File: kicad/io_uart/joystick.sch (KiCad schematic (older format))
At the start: 8 parts

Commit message: cleanup
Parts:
- gave numbers to parts that had none: 3
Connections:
- net /JOYPORT_ENABLE: now also U2.5, U2.9; no longer U2.10, U2.12
- net JOYPORT_SELECT: now also U2.1, U2.2, U2.4; no longer U2.4, U2.5, U2.9
- net at U3.19 (OEb), U4.1 (EN): now also U2.6; no longer U2.8
- net at U3.1 (OEa), U4.4 (EN): now also U2.8; no longer U2.11
- new net: U2.10, U2.3
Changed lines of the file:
@@
 	6100 3900 7250 3900
 $Comp
-L 7400 U?
-U 2 1 58E419A1
+L 7400 U2
+U 1 1 58E419A1
 P 3700 3450
-F 0 "U?" H 3700 3500 50  0000 C CNN
+F 0 "U2" H 3700 3500 50  0000 C CNN
 F 1 "7400" H 3700 3350 50  0000 C CNN
 F 2 "" H 3700 3450 50  0000 C CNN
 F 3 "" H 3700 3450 50  0000 C CNN
-	2    3700 3450
-	1    0    0    -1
-$EndComp
-$Comp
-L 7400 U?
-U 3 1 58E41A5A
+	1    3700 3450
+	1    0    0    -1
+$EndComp
+$Comp
+L 7400 U2
+U 2 1 58E41A5A
 P 5050 2800
-F 0 "U?" H 5050 2850 50  0000 C CNN
+F 0 "U2" H 5050 2850 50  0000 C CNN
 F 1 "7400" H 5050 2700 50  0000 C CNN
 F 2 "" H 5050 2800 50  0000 C CNN
 F 3 "" H 5050 2800 50  0000 C CNN
-	3    5050 2800
-	1    0    0    -1
-$EndComp
-$Comp
-L 7400 U?
-U 4 1 58E41B17
+	2    5050 2800
+	1    0    0    -1
+$EndComp
+$Comp
+L 7400 U2
+U 3 1 58E41B17
 P 5050 3350
-F 0 "U?" H 5050 3400 50  0000 C CNN
+F 0 "U2" H 5050 3400 50  0000 C CNN
 F 1 "7400" H 5050 3250 50  0000 C CNN
 F 2 "" H 5050 3350 50  0000 C CNN
 F 3 "" H 5050 3350 50  0000 C CNN
-	4    5050 3350
-	1    0    0    -1
-$EndComp
-$Comp
-L 74LS244 U?
+	3    5050 3350
+	1    0    0    -1
+$EndComp
+$Comp
+L 74LS244 U3
 U 1 1 58E41D13
 P 7950 3400
-F 0 "U?" H 8000 3200 50  0000 C CNN
+F 0 "U3" H 8000 3200 50  0000 C CNN
 F 1 "74LS244" H 8050 3000 50  0000 C CNN
 F 2 "" H 7950 3400 50  0000 C CNN
@@
 Connection ~ 6850 3600
 $Comp
-L 74125 U?
+L 74125 U4
 U 1 1 58E447D4
 P 7900 2400
-F 0 "U?" H 8150 2650 50  0000 L BNN
+F 0 "U4" H 8150 2650 50  0000 L BNN
 F 1 "74125" H 8000 2100 40  0000 L TNN
 F 2 "Housings_DIP:DIP-14_W7.62mm_LongPads" H 7900 2400 60  0001 C CNN
@@
 $EndComp
 $Comp
-L 74125 U?
+L 74125 U4
 U 2 1 58E44BAD
 P 7900 4400
-F 0 "U?" H 8150 4650 50  0000 L BNN
+F 0 "U4" H 8150 4650 50  0000 L BNN
 F 1 "74125" H 8000 4100 40  0000 L TNN
 F 2 "Housings_DIP:DIP-14_W7.62mm_LongPads" H 7900 4400 60  0001 C CNN
@@
 	8900 2800 9900 2800
 $Comp
-L GND #PWR?
+L GND #PWR035
 U 1 1 58E4818B
 P 9800 4600
-F 0 "#PWR?" H 9800 4350 50  0001 C CNN
+F 0 "#PWR035" H 9800 4350 50  0001 C CNN
 F 1 "GND" H 9800 4450 50  0000 C CNN
 F 2 "" H 9800 4600 50  0000 C CNN
@@
 Connection ~ 6700 2400
 $Comp
-L VCC #PWR?
+L VCC #PWR036
 U 1 1 58E55481
 P 9700 1750
-F 0 "#PWR?" H 9700 1600 50  0001 C CNN
+F 0 "#PWR036" H 9700 1600 50  0001 C CNN
 F 1 "VCC" H 9700 1900 50  0000 C CNN
 F 2 "" H 9700 1750 50  0000 C CNN

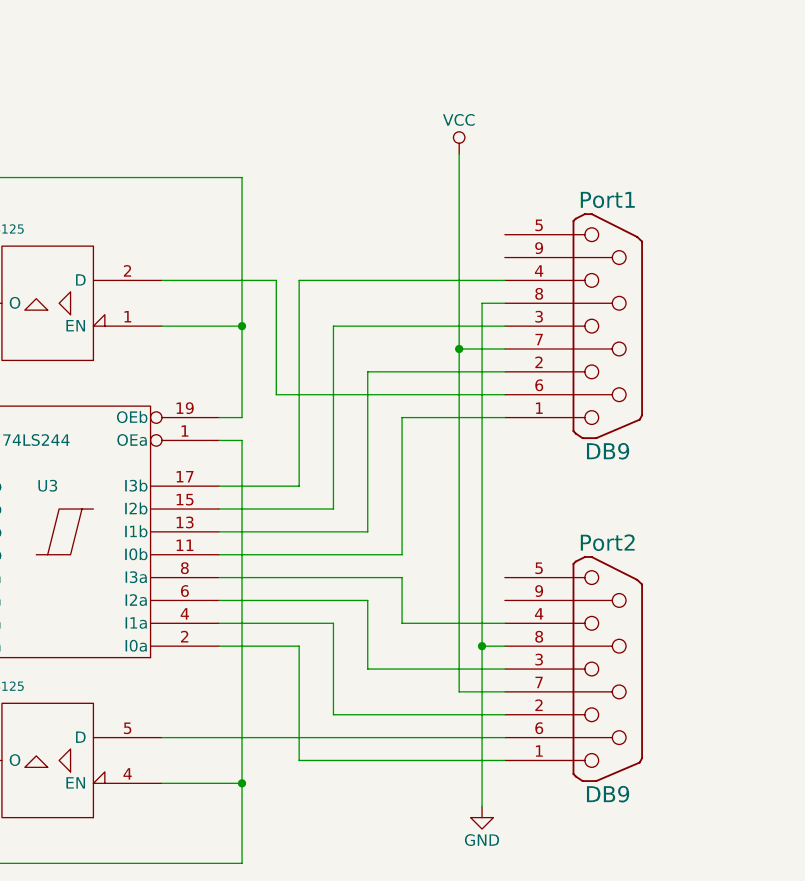
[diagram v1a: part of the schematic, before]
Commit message: new joystick interface
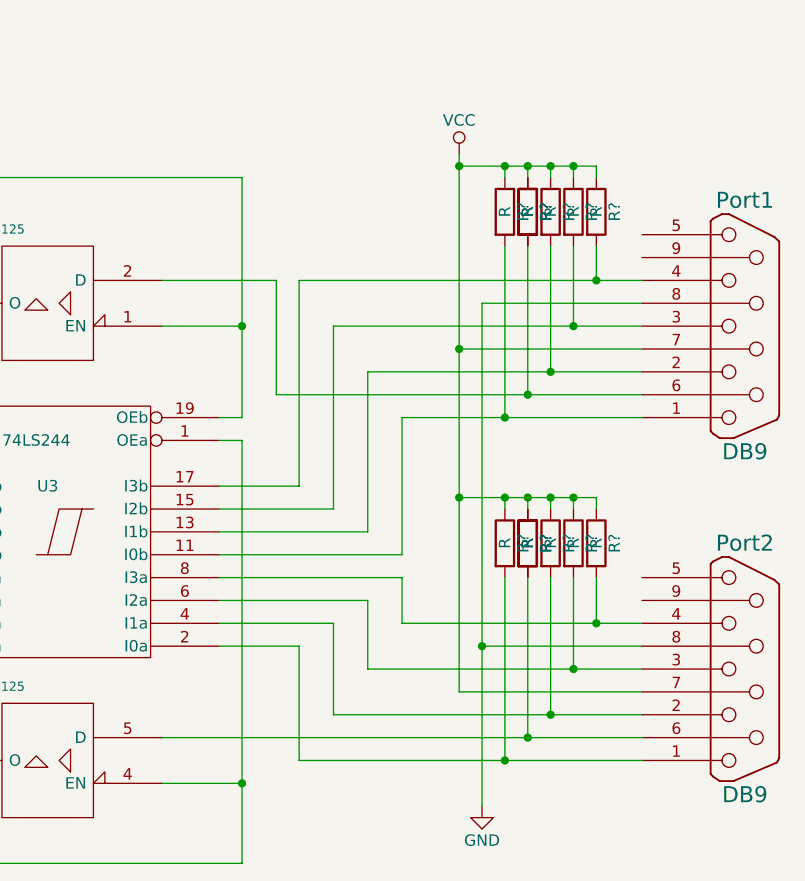
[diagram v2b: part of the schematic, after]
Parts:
- added R? (x12): R, symbol R
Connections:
- net VCC: now also R?.1, R?.1, R?.1, R?.1, R?.1, R?.1, R?.1, R?.1, R?.1, R?.1, R?.1, R?.1
- net at Port1.1, U3.11 (I0b): now also R?.2
- net at Port1.2, U3.13 (I1b): now also R?.2
- net at Port1.3, U3.15 (I2b): now also R?.2
- net at Port1.4, U3.17 (I3b): now also R?.2
- net at Port1.6 (P6), U4.2 (D): now also R?.2, R?.2
- net at Port2.1, U3.2 (I0a): now also R?.2
- net at Port2.2, U3.4 (I1a): now also R?.2
- net at Port2.3, U3.6 (I2a): now also R?.2
- net at Port2.4, U3.8 (I3a): now also R?.2
- net at Port2.6 (P6), U4.5 (D): now also R?.2, R?.2
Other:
- moved on the sheet: Port1, Port2

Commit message: xmodem
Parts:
- removed R? (x12): R, symbol R
- added R20, R21: 1k, Discret:R3-LARGE_PADS, symbol R
- added RR1: 1k, Resistors_ThroughHole:Resistor_Array_SIP8, symbol RR8
- U2: footprint (none) -> Housings_DIP:DIP-14_W7.62mm_LongPads
- U3: footprint (none) -> Housings_DIP:DIP-20_W7.62mm_LongPads
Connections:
- net VCC: now also R20.2, R21.2, RR1.1 (COM)
- net at Port1.1, U3.11 (I0b): now also RR1.2
- net at Port1.2, U3.13 (I1b): now also RR1.4
- net at Port1.3, U3.15 (I2b): now also RR1.5
- net at Port1.4, U3.17 (I3b): now also RR1.6
- net at Port1.6 (P6), U4.2 (D): now also RR1.3
- net at Port2.1, U3.2 (I0a): now also R20.1
- net at Port2.2, U3.4 (I1a): now also RR1.7
- net at Port2.3, U3.6 (I2a): now also RR1.8
- net at Port2.4, U3.8 (I3a): now also RR1.9
- net at Port2.6 (P6), U4.5 (D): now also R21.1
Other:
- moved on the sheet: Port1, Port2, U2A, U2B, U2C, U3, U4A, U4B

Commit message: io board release candidate
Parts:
- R20, R21: footprint Discret:R3-LARGE_PADS -> Resistors_ThroughHole:Resistor_Horizontal_RM7mm
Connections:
- no-connect marks 0 -> 4
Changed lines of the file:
@@
 F 0 "R20" V 8680 5400 50  0000 C CNN
 F 1 "1k" V 8600 5400 50  0000 C CNN
-F 2 "Discret:R3-LARGE_PADS" V 8530 5400 50  0001 C CNN
+F 2 "Resistors_ThroughHole:Resistor_Horizontal_RM7mm" V 8530 5400 50  0001 C CNN
 F 3 "" H 8600 5400 50  0000 C CNN
 	1    8600 5400
@@
 F 0 "R21" V 8780 5400 50  0000 C CNN
 F 1 "1k" V 8700 5400 50  0000 C CNN
-F 2 "Discret:R3-LARGE_PADS" V 8630 5400 50  0001 C CNN
+F 2 "Resistors_ThroughHole:Resistor_Horizontal_RM7mm" V 8630 5400 50  0001 C CNN
 F 3 "" H 8700 5400 50  0000 C CNN
 	1    8700 5400
@@
 	9100 2350 9100 4600
 Connection ~ 9100 4600
+NoConn ~ 10300 2500
+NoConn ~ 10300 2600
+NoConn ~ 10300 4000
+NoConn ~ 10300 4100
 $EndSCHEMATC

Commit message: cleanup
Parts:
- Port1, Port2: symbol DB9 -> io-rescue:DB9
- R20, R21: symbol R -> io-rescue:R
- RR1: symbol RR8 -> io-rescue:RR8
- U2: symbol 7400 -> io-rescue:7400
- U3: symbol 74LS244 -> io-rescue:74LS244
- U4: symbol 74125 -> io-rescue:74125
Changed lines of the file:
@@
-EESchema Schematic File Version 2
-LIBS:io-rescue
-LIBS:power
-LIBS:device
-LIBS:transistors
-LIBS:conn
-LIBS:linear
-LIBS:regul
-LIBS:74xx
-LIBS:cmos4000
-LIBS:adc-dac
-LIBS:memory
-LIBS:xilinx
-LIBS:microcontrollers
-LIBS:dsp
-LIBS:microchip
-LIBS:analog_switches
-LIBS:motorola
-LIBS:texas
-LIBS:intel
-LIBS:audio
-LIBS:interface
-LIBS:digital-audio
-LIBS:philips
-LIBS:display
-LIBS:cypress
-LIBS:siliconi
-LIBS:opto
-LIBS:atmel
-LIBS:contrib
-LIBS:valves
-LIBS:65xxx
-LIBS:ttl_ieee
-LIBS:mini_din
-LIBS:dallas-rtc
-LIBS:lp2950l
-LIBS:osc
-LIBS:io-cache
-EELAYER 25 0
+EESchema Schematic File Version 4
+EELAYER 30 0
 EELAYER END
 $Descr A4 11693 8268
@@
 $EndDescr
 $Comp
-L DB9 Port1
+L io-rescue:DB9 Port1
 U 1 1 54318EBC
 P 10750 2900
@@
 $EndComp
 $Comp
-L DB9 Port2
+L io-rescue:DB9 Port2
 U 1 1 54318F7A
 P 10750 4400
@@
 1,2V U_Fwd. + 0,7V U_Sperr + 0,1V U_CE = 2V \n5V - 2V = 3V --> R=U/I \n-> R_max = 3V/0,005A I_Fwd. = 600 Ohm\n-> R_min = 3V/0,05A I_CE_max = 60 Ohm
 $Comp
-L 7400 U2
+L io-rescue:7400 U2
 U 1 1 58E419A1
 P 2400 3850
@@
 $EndComp
 $Comp
-L 7400 U2
+L io-rescue:7400 U2
 U 2 1 58E41A5A
 P 3750 3200
@@
 $EndComp
 $Comp
-L 7400 U2
+L io-rescue:7400 U2
 U 3 1 58E41B17
 P 3750 3750
@@
 $EndComp
 $Comp
-L 74LS244 U3
+L io-rescue:74LS244 U3
 U 1 1 58E41D13
 P 6650 3800
@@
 $EndComp
 $Comp
-L 74125 U4
+L io-rescue:74125 U4
 U 1 1 58E447D4
 P 6600 2800
@@
 $EndComp
 $Comp
-L 74125 U4
+L io-rescue:74125 U4
 U 2 1 58E44BAD
 P 6600 4800
@@
 $EndComp
 $Comp
-L GND #PWR035
+L io-rescue:GND #PWR035
 U 1 1 58E4818B
 P 8500 5000
@@
 JOYPORT_SELECT
 $Comp
-L VCC #PWR036
+L io-rescue:VCC #PWR036
 U 1 1 58E55481
 P 8400 2150
@@
 $EndComp
 $Comp
-L RR8 RR1
+L io-rescue:RR8 RR1
 U 1 1 597CB088
 P 8950 2000
@@
 $EndComp
 $Comp
-L R R20
+L io-rescue:R R20
 U 1 1 597DB3E5
 P 8600 5400
@@
 $EndComp
 $Comp
-L R R21
+L io-rescue:R R21
 U 1 1 597DB45C
 P 8700 5400
